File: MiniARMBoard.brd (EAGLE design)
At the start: 38.2 x 23.1 mm, 37 parts, among them CN1 J_USB_MICROAB_HIROSE_ZX62-AB-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, U1 LPC1549JBD48, U2 FT232RQ, U3 MCP1700T-33, U4 ADR5041, X1 FA238V

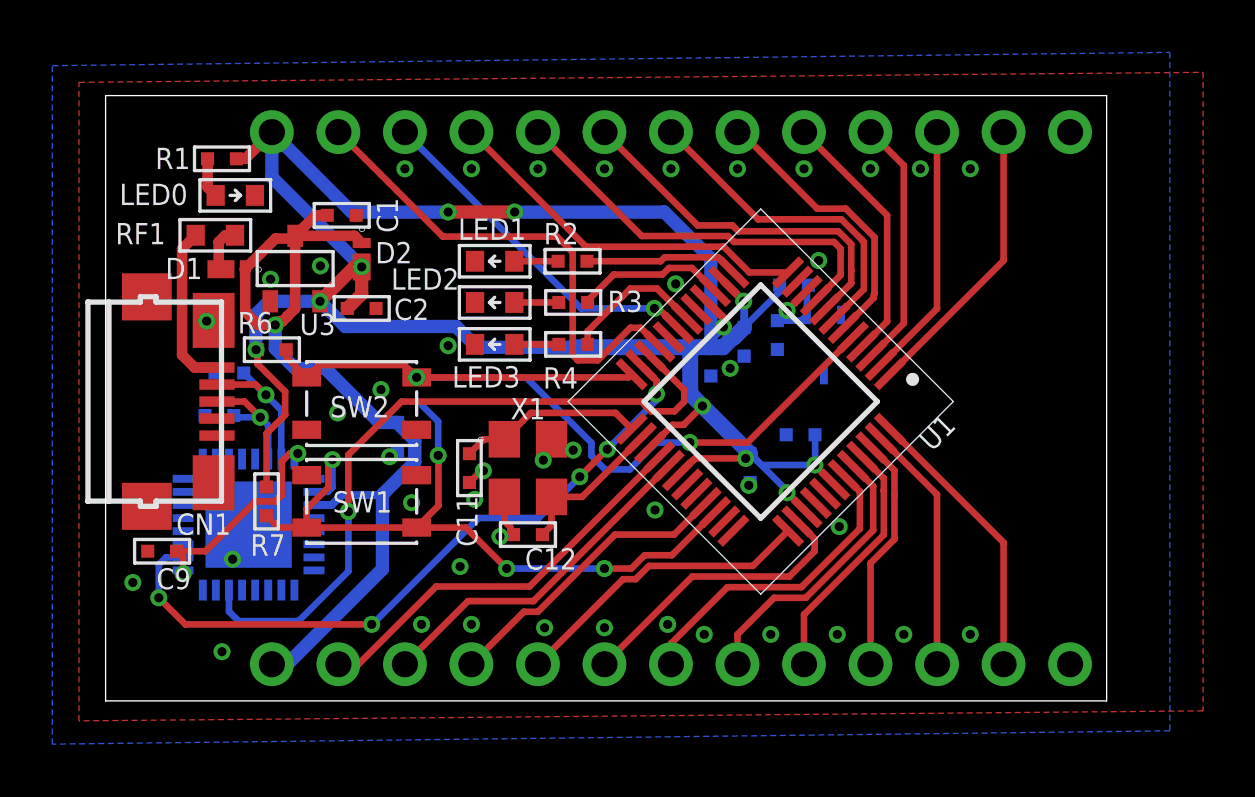
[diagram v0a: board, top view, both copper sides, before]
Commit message: パーツ変更
USBの保護をRFからICに
シリアル変換ICをFT234XDに
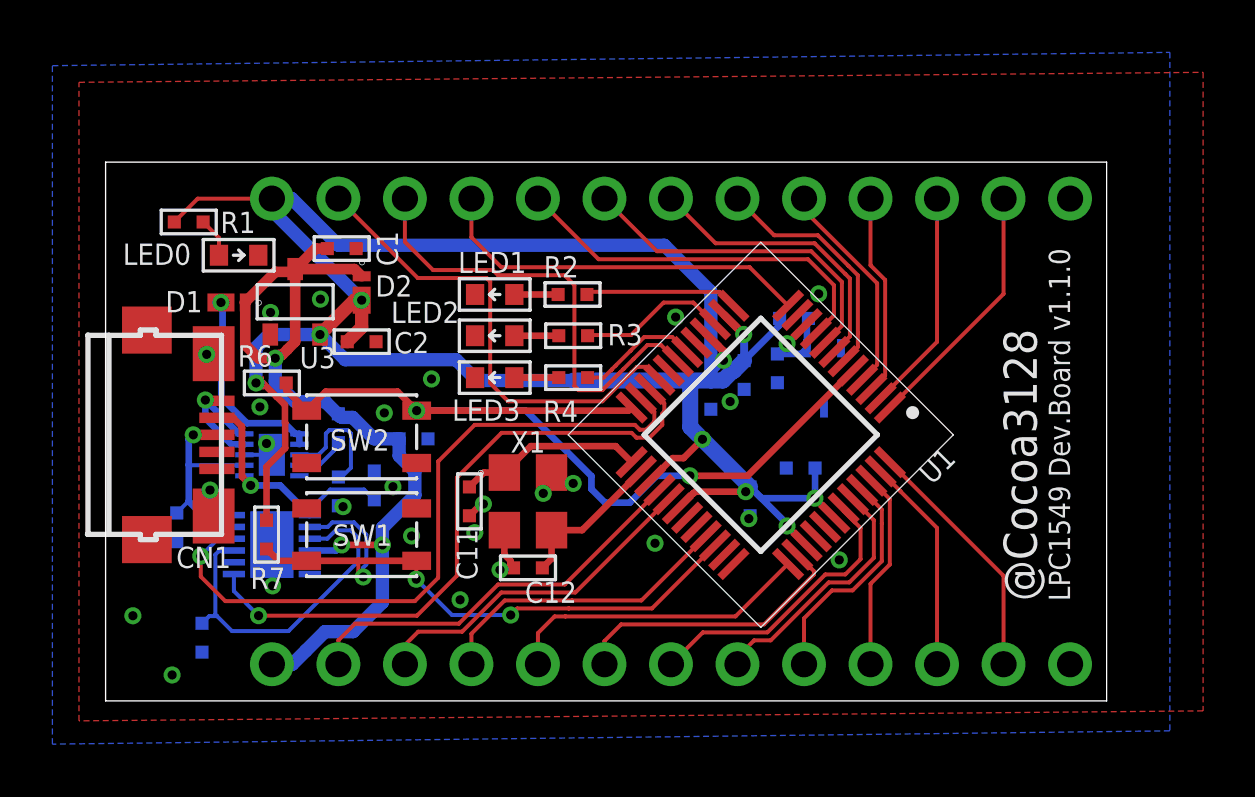
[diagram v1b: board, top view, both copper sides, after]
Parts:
- removed RF1: (no value), Passive:1608
- removed U2: FT232RQ, FT232RQ:QFN50P500X500X100-33N
- added IC1: TPD4S014DSQR, TPD4S014DSQR:SON40P200X200X80-11N
- added IC2: FT234XD-R, FT234XD-R:SON45P300X300X75-13N
- added R8, R9: 10k, MotorDriver:R1005
- moved C7 6.49 mm to (10.3, 8.23), turned to 90 degrees
- moved C8 6.23 mm to (2.72, 6.63), turned to 270 degrees
- moved C9 3.64 mm to (3.68, 2.41), flipped to the bottom, turned to 270 degrees
- moved R1 2.73 mm to (3.17, 18.3), turned to 180 degrees
- moved CN2 2.54 mm to (22.9, 19.2)
- moved LED0 2.29 mm to (5.08, 17.0)
- moved C1 1.27 mm to (9.02, 17.3)
- moved C2 1.27 mm to (9.78, 13.7)
- moved C4 1.27 mm to (23.1, 11.7)
- moved C6 1.27 mm to (25.7, 12.7)
- moved D2 1.27 mm to (9.78, 15.6)
- moved LED1 1.27 mm to (14.9, 15.5)
- moved LED2 1.27 mm to (14.9, 13.9)
- moved R2 1.27 mm to (17.8, 15.5)
- moved R3 1.27 mm to (17.9, 13.9)
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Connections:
- removed net N$11: C9.1, U2.1, U2.16
- new net N$4: C9.1, IC2.3, IC2.9
- new net N$6: IC1.3, R8.2
- new net N$7: IC1.4, R9.1
- net !RESET: now also IC2.2; no longer U2.18
- net +5V: now also IC2.4, R9.2; no longer U2.19
- net D+: now also C8.1, IC1.7, IC2.12; no longer C7.1, U2.14
- net D-: now also C7.1, IC1.6, IC2.1; no longer C8.1, U2.15
- net GND: now also IC1.11, IC1.8, IC2.13, IC2.5, R8.1; no longer U2.17, U2.20, U2.24, U2.26, U2.33, U2.4
- net N$3: now also IC1.1, IC1.2; no longer RF1.2
- net N$56: now also IC1.10, IC1.9; no longer RF1.1
- net RX: now also IC2.7; no longer U2.30
- net TX: now also IC2.10; no longer U2.2
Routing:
- net N$4: track 0.00 -> 13.6 mm
- net N$11: track 8.39 -> 0.00 mm, vias 2 -> 0
- net N$3: track 1.81 -> 7.76 mm, vias 0 -> 1
- net N$6: track 0.00 -> 4.65 mm
- net !RESET: track 28.9 -> 24.5 mm, vias 4 -> 3
- net PIO0_12: track 13.5 -> 17.7 mm, vias 1 -> 0
- net D-: track 5.93 -> 9.82 mm
- net D+: track 4.67 -> 8.23 mm
- net GND: track 2.30 -> 5.08 mm, vias 43 -> 26
- net RX: track 27.0 -> 24.4 mm
- net N$7: track 0.00 -> 1.93 mm
- net PIO0_2: track 9.58 -> 7.72 mm
- net PIO0_3: track 9.90 -> 8.31 mm
- net PIO0_5: track 10.8 -> 9.32 mm
- net PIO0_27: track 9.02 -> 7.61 mm
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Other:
- board size 38.2 x 23.1 mm -> 38.2 x 20.6 mm
- board text added: "LPC1549 Dev.Board v1.1.0"
- board text removed: "LPC1549 Dev.Board v1.0.0"

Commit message: 集積化を進めた
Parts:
- moved CN2 3.81 mm to (19.1, 19.2)
- moved CN3 3.81 mm to (16.5, 1.40)
- moved R1 2.36 mm to (1.27, 16.9), turned to 90 degrees
- moved LED0 1.85 mm to (3.30, 16.5)
- moved C9 1.73 mm to (3.17, 4.06), flipped to the top, turned to 180 degrees
- moved R6 0.25 mm to (6.60, 12.1)
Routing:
- net PIO0_8: track 14.8 -> 19.3 mm
- net PIO0_7: track 13.0 -> 17.4 mm
- net PIO0_6: track 11.1 -> 15.6 mm
- net PIO0_13: track 18.5 -> 22.5 mm
- net +3V3: track 87.7 -> 91.7 mm
- net PIO0_5: track 9.32 -> 13.3 mm
- net PIO0_24: track 11.1 -> 15.0 mm
- net PIO0_3: track 8.31 -> 12.0 mm
- net PIO0_25: track 9.62 -> 13.3 mm
- net PIO0_23: track 11.0 -> 14.5 mm
- net PIO0_22: track 11.8 -> 15.3 mm
- net +5V: track 35.4 -> 38.8 mm
- net PIO0_19: track 13.1 -> 16.5 mm
- net PIO0_12: track 17.7 -> 21.0 mm
- net PIO0_17: track 15.6 -> 18.8 mm
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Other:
- board size 38.2 x 20.6 mm -> 35.6 x 20.6 mm
